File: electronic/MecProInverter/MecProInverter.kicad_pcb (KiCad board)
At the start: 4 copper layers, 104 x 175 mm, 39 parts, among them J1 0022232031, J2 0022232031, J4 Screw_Terminal_01x08, J5 Conn_01x08, J6 LM61, J7 Conn_01x11, K2 RT314A12, Q1 DMN3404L, Q2 DMN3404L, SW1 PTS645SM95SMTR92LFS, SW2 PTS645SM95SMTR92LFS, SW3 PTS645SM95SMTR92LFS, U1 ESP32-S3-MINI-1-N8, U10 CC6904SO-30A, U11 CC6904SO-30A, U12 ACS722xLCTR-40AB, U13 IKCM20L60GA, U14 PSRV05-4MR6T1G, U15 ADUM1201ARZ-RL7, U16 ADUM1201ARZ-RL7, U17 PSRV05-4MR6T1G, U18 PMV100EPAR, U2 ADUM3160, U3 TYPE-C_16PIN_2MD(073), U5 TPS563201DDCR, U6 SKRKAEE020, U7 SKRKAEE020, U8 TLA2528IRTER, U9 CC6904SO-30A

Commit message: Electronic
Power Terminal edit
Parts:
- added D1: LED_3.3V, LED_SMD:LED_0603_1608Metric, F.Cu at (68.7, 169.5)
- added D2: LED_15V, LED_SMD:LED_0603_1608Metric, F.Cu at (68.7, 172.1)
- added H1: MountingHole_Pad, MountingHole:MountingHole_3.2mm_M3_DIN965_Pad_TopBottom, F.Cu at (99.0, 223.0)
- added H2: MountingHole_Pad, MountingHole:MountingHole_3.2mm_M3_DIN965_Pad_TopBottom, F.Cu at (65.6, 164.6)
- added H3: MountingHole_Pad, MountingHole:MountingHole_3.2mm_M3_DIN965_Pad_TopBottom, F.Cu at (193.0, 223.0)
- added H4: MountingHole_Pad, MountingHole:MountingHole_3.2mm_M3_DIN965_Pad_TopBottom, F.Cu at (72.8, 164.6)
- added H5: MountingHole_Pad, MountingHole:MountingHole_3.2mm_M3_DIN965_Pad_TopBottom, F.Cu at (79.9, 157.5)
- added H6: MountingHole_Pad, MountingHole:MountingHole_3.2mm_M3_DIN965_Pad_TopBottom, F.Cu at (79.9, 164.6)
- added J10: Screw_Terminal_01x04, Connector_Phoenix_MC_HighVoltage:PhoenixContact_MCV_1,5_4-G-5.08_1x04_P5.08mm_Vertical, F.Cu at (130.9, 223.7)
- added J3: Screw_Terminal_01x06, Connector_Phoenix_MC_HighVoltage:PhoenixContact_MCV_1,5_6-G-5.08_1x06_P5.08mm_Vertical, F.Cu at (144.3, 251.7)
- added J8: Conn_01x01, Connector_PinHeader_2.54mm:PinHeader_1x01_P2.54mm_Vertical, F.Cu at (64.4, 170.5)
- added J9: Conn_01x01, Connector_PinHeader_2.54mm:PinHeader_1x01_P2.54mm_Vertical, F.Cu at (64.4, 175.2)
- added RV1: 10K, Potentiometer_THT:Potentiometer_Alps_RK09K_Single_Vertical, F.Cu at (98.0, 102.5)
- added TP5: MTCK, TestPoint:TestPoint_Pad_D2.0mm, F.Cu at (53.0, 195.8)
- added TP6: MTDO, TestPoint:TestPoint_Pad_D2.0mm, F.Cu at (53.0, 199.9)
- added TP7: MTMS, TestPoint:TestPoint_Pad_D2.0mm, F.Cu at (53.0, 203.9)
- added TP8: MTDI, TestPoint:TestPoint_Pad_D2.0mm, F.Cu at (53.0, 208.0)
- added U19: PSRV05-4MR6T1G, footprint:SOT-23-6_L2.9-W1.6-P0.95-LS2.8-BL, F.Cu at (48.9, 196.0)
- added U20: PSRV05-4MR6T1G, footprint:SOT-23-6_L2.9-W1.6-P0.95-LS2.8-BL, F.Cu at (48.9, 200.6)
- added U4: LVE2560E, Own_Library:LVE2560E, B.Cu at (140.5, 211.2)
- J1, J2: footprint digikey-footprints:PinHeader_1x3_P2.54mm_Drill1.02mm -> footprint:CONN-TH_3P-P2.54_22-23-2031
- J4: value Screw_Terminal_01x08 -> Screw_Terminal_01x04; footprint Connector_Phoenix_MC_HighVoltage:PhoenixContact_MCV_1,5_8-G-5.08_1x08_P5.08mm_Vertical -> Connector_Phoenix_MC_HighVoltage:PhoenixContact_MCV_1,5_4-G-5.08_1x04_P5.08mm_Vertical
- TP1, TP2, TP3, TP4: footprint Connector_Pin:Pin_D1.0mm_L10.0mm_LooseFit -> TestPoint:TestPoint_Pad_D2.0mm
- U12: value ACS722xLCTR-40AB -> TEA1-0505HI; footprint Package_SO:SOIC-8_3.9x4.9mm_P1.27mm -> Converter_DCDC:Converter_DCDC_TRACO_TEA1HI-xxxx_THT
- moved U12 34.3 mm to (169.5, 214.0), turned to -90 degrees
- moved Q1 30.1 mm to (151.0, 193.0)
- moved D3 17.4 mm to (107.0, 89.0)
- moved U9 17.3 mm to (102.0, 212.0)
- moved U13 16.0 mm to (133.0, 167.0)
- moved PS1 3.00 mm to (102.2, 122.7)
- moved U10 2.24 mm to (102.0, 206.0)
- moved U2 1.00 mm to (182.0, 213.0)
- moved J4 0.34 mm to (108.6, 223.7)
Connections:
- net Net-(U12-VIOUT) renamed +5V
- C2 pad 1: Net-(U13-P) -> Net-(J8-Pin_1)
- C3 pad 1: Net-(U13-P) -> Net-(J8-Pin_1)
- C4 pad 1: Net-(U13-P) -> Net-(J8-Pin_1)
- J4 pad 1: /Power/AC_L -> GND
- J4 pad 2: /Power/AC_N -> /Power/W
- J4 pad 3: Earth -> /Power/V
- J4 pad 4: Earth -> /Power/U
- J7 pad 8: unconnected-(J7-Pin_8-Pad8) -> /Control/UART_TX
- J7 pad 9: unconnected-(J7-Pin_9-Pad9) -> /Control/UART_RX
- U1 pad 10: /Control/FAN1_PWM_FB -> /Control/SW2OUT
- U1 pad 11: /Control/POT1OUT -> /Control/SW3OUT
- U1 pad 12: /Control/RGBLED -> Net-(U1-IO8)
- U1 pad 13: LINW -> Net-(U1-IO9)
- U1 pad 14: LINV -> LINW
- U1 pad 15: LINU -> LINV
- U1 pad 16: HINW -> LINU
- U1 pad 17: HINV -> HINW
- U1 pad 18: HINU -> HINV
- U1 pad 19: RELAY -> HINU
- U1 pad 20: /Control/TEMP_HEATSINK -> RELAY
- U1 pad 21: Net-(U1-IO17) -> /Control/RGBLED
- U1 pad 22: Net-(U1-IO18) -> /Control/TEMP_HEATSINK
- U1 pad 25: unconnected-(U1-IO21-Pad25) -> /Control/ISO_GPIO_1
- U1 pad 26: /Control/SW1OUT -> unconnected-(U1-IO26-Pad26)
- U1 pad 27: unconnected-(U1-IO47-Pad27) -> VFO
- U1 pad 28: /Control/SW2OUT -> ITRIP
- U1 pad 29: /Control/SW3OUT -> /Control/SPI_CS
- U1 pad 31: /Control/SPI_MISO -> /Control/SPI_MOSI
- U1 pad 32: /Control/SPI_MOSI -> /Control/SPI_CLK
- U1 pad 33: /Control/SPI_CLK -> /Control/SPI_MISO
- U1 pad 34: /Control/SPI_CS -> /Control/ISO_GPIO_2
- U1 pad 35: unconnected-(U1-IO39-Pad35) -> Net-(U1-IO39)
- U1 pad 36: unconnected-(U1-IO40-Pad36) -> Net-(U1-IO40)
- U1 pad 37: unconnected-(U1-IO41-Pad37) -> Net-(U1-IO41)
- U1 pad 38: unconnected-(U1-IO42-Pad38) -> Net-(U1-IO42)
- U1 pad 5: unconnected-(U1-IO1-Pad5) -> /Control/FAN_CONTROL
- U1 pad 6: unconnected-(U1-IO2-Pad6) -> /Control/FAN1_PWM_FB
- U1 pad 7: unconnected-(U1-IO3-Pad7) -> /Control/FAN2_PWM_FB
- U1 pad 8: /Control/FAN_CONTROL -> /Control/POT1OUT
- U1 pad 9: /Control/FAN2_PWM_FB -> /Control/SW1OUT
- U12 pad 1: Net-(U13-U) -> +5VD
- U12 pad 2: Net-(U13-U) -> GNDD
- U13 pad 14: unconnected-(U13-VFO-Pad14) -> VFO
- U13 pad 15: unconnected-(U13-ITRIP-Pad15) -> ITRIP
- U13 pad 23: Net-(U13-P) -> Net-(J8-Pin_1)
- U16 pad 2: /Control/ISO_GPIO_3 -> /Control/UART_RX
- U16 pad 3: /Control/ISO_GPIO_4 -> /Control/UART_TX
- U8 pad 6: Net-(U8-AIN7/GPIO7) -> unconnected-(U8-AIN7/GPIO7-Pad6)
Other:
- outline, holes or cut-outs redrawn

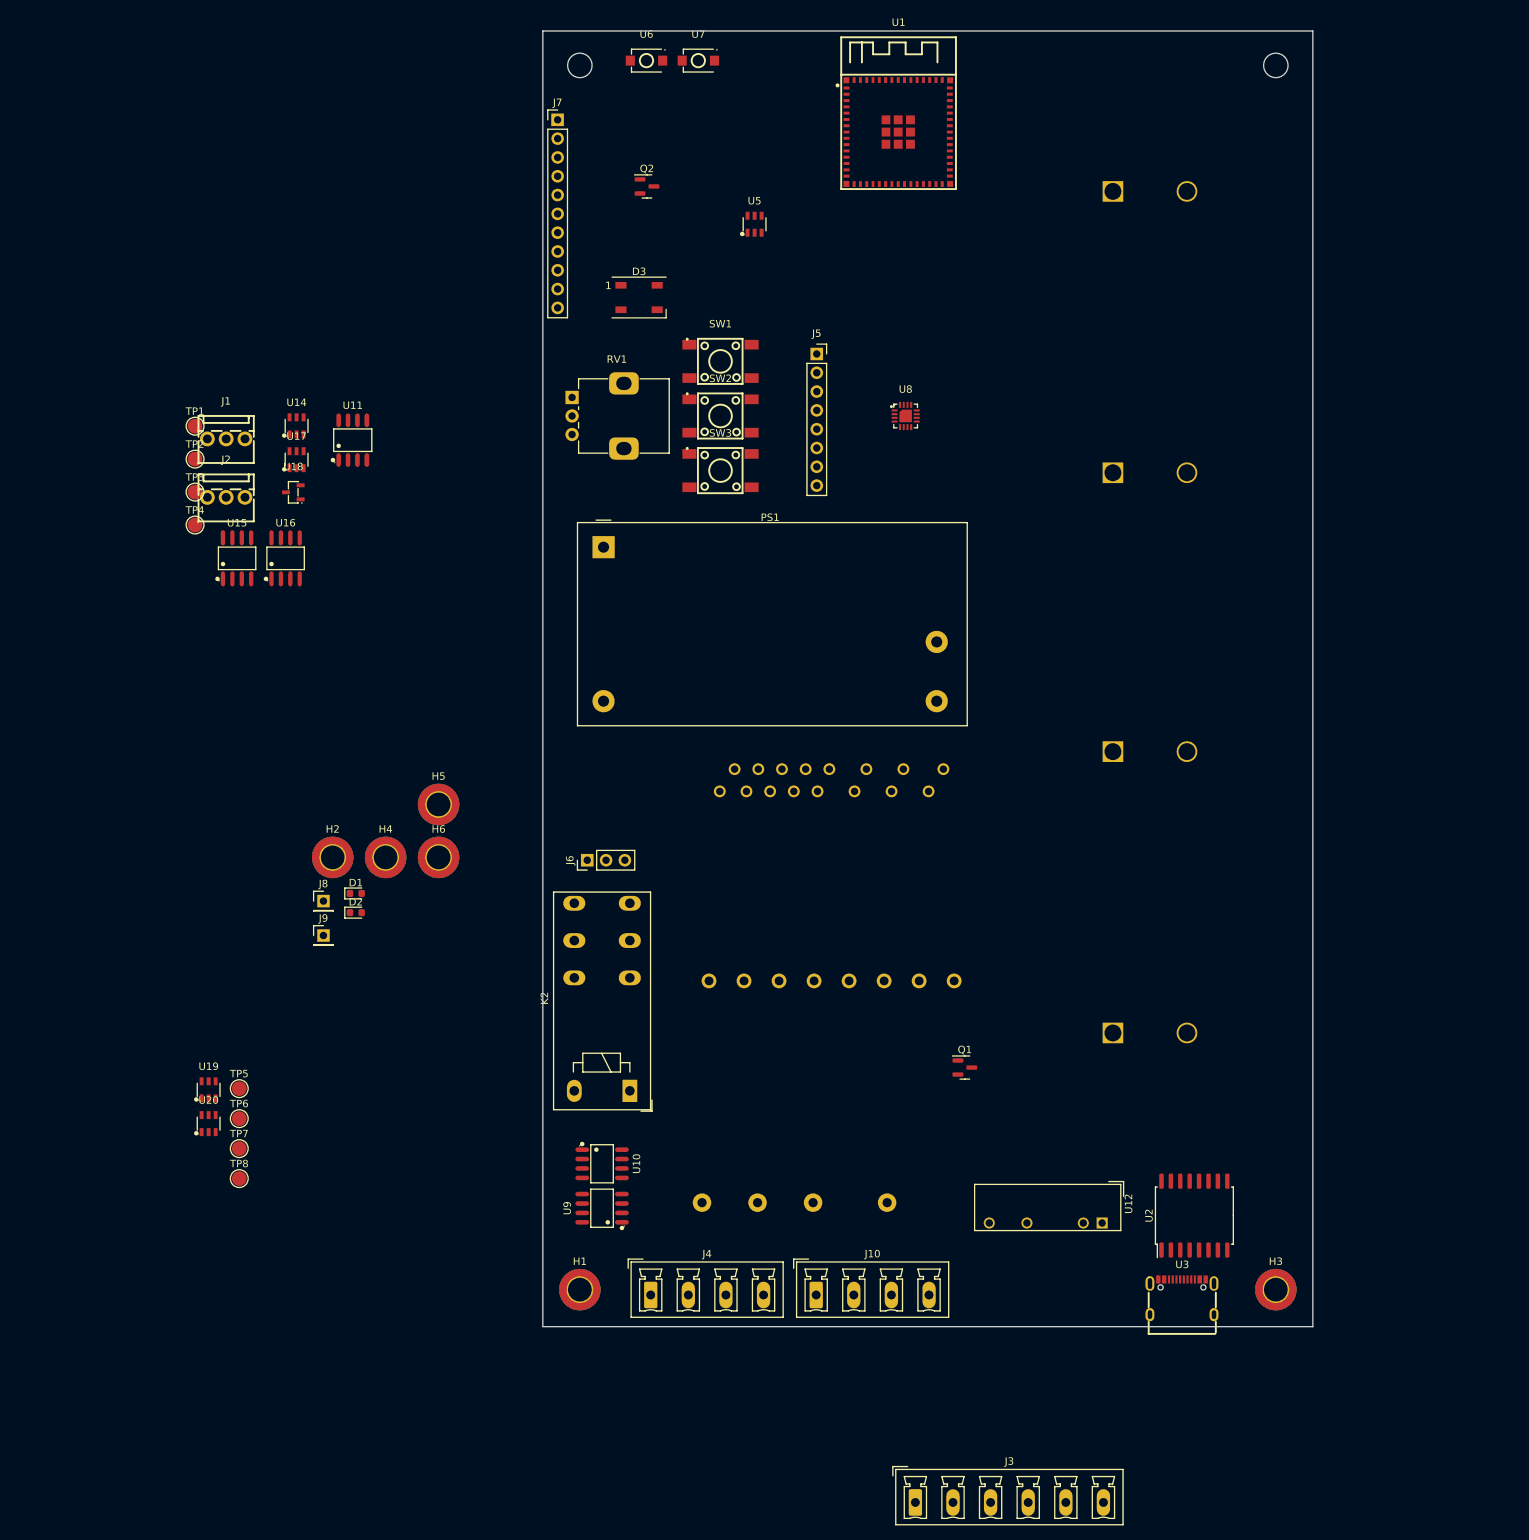
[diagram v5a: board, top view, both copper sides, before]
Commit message: Electronic
Footprint assignment
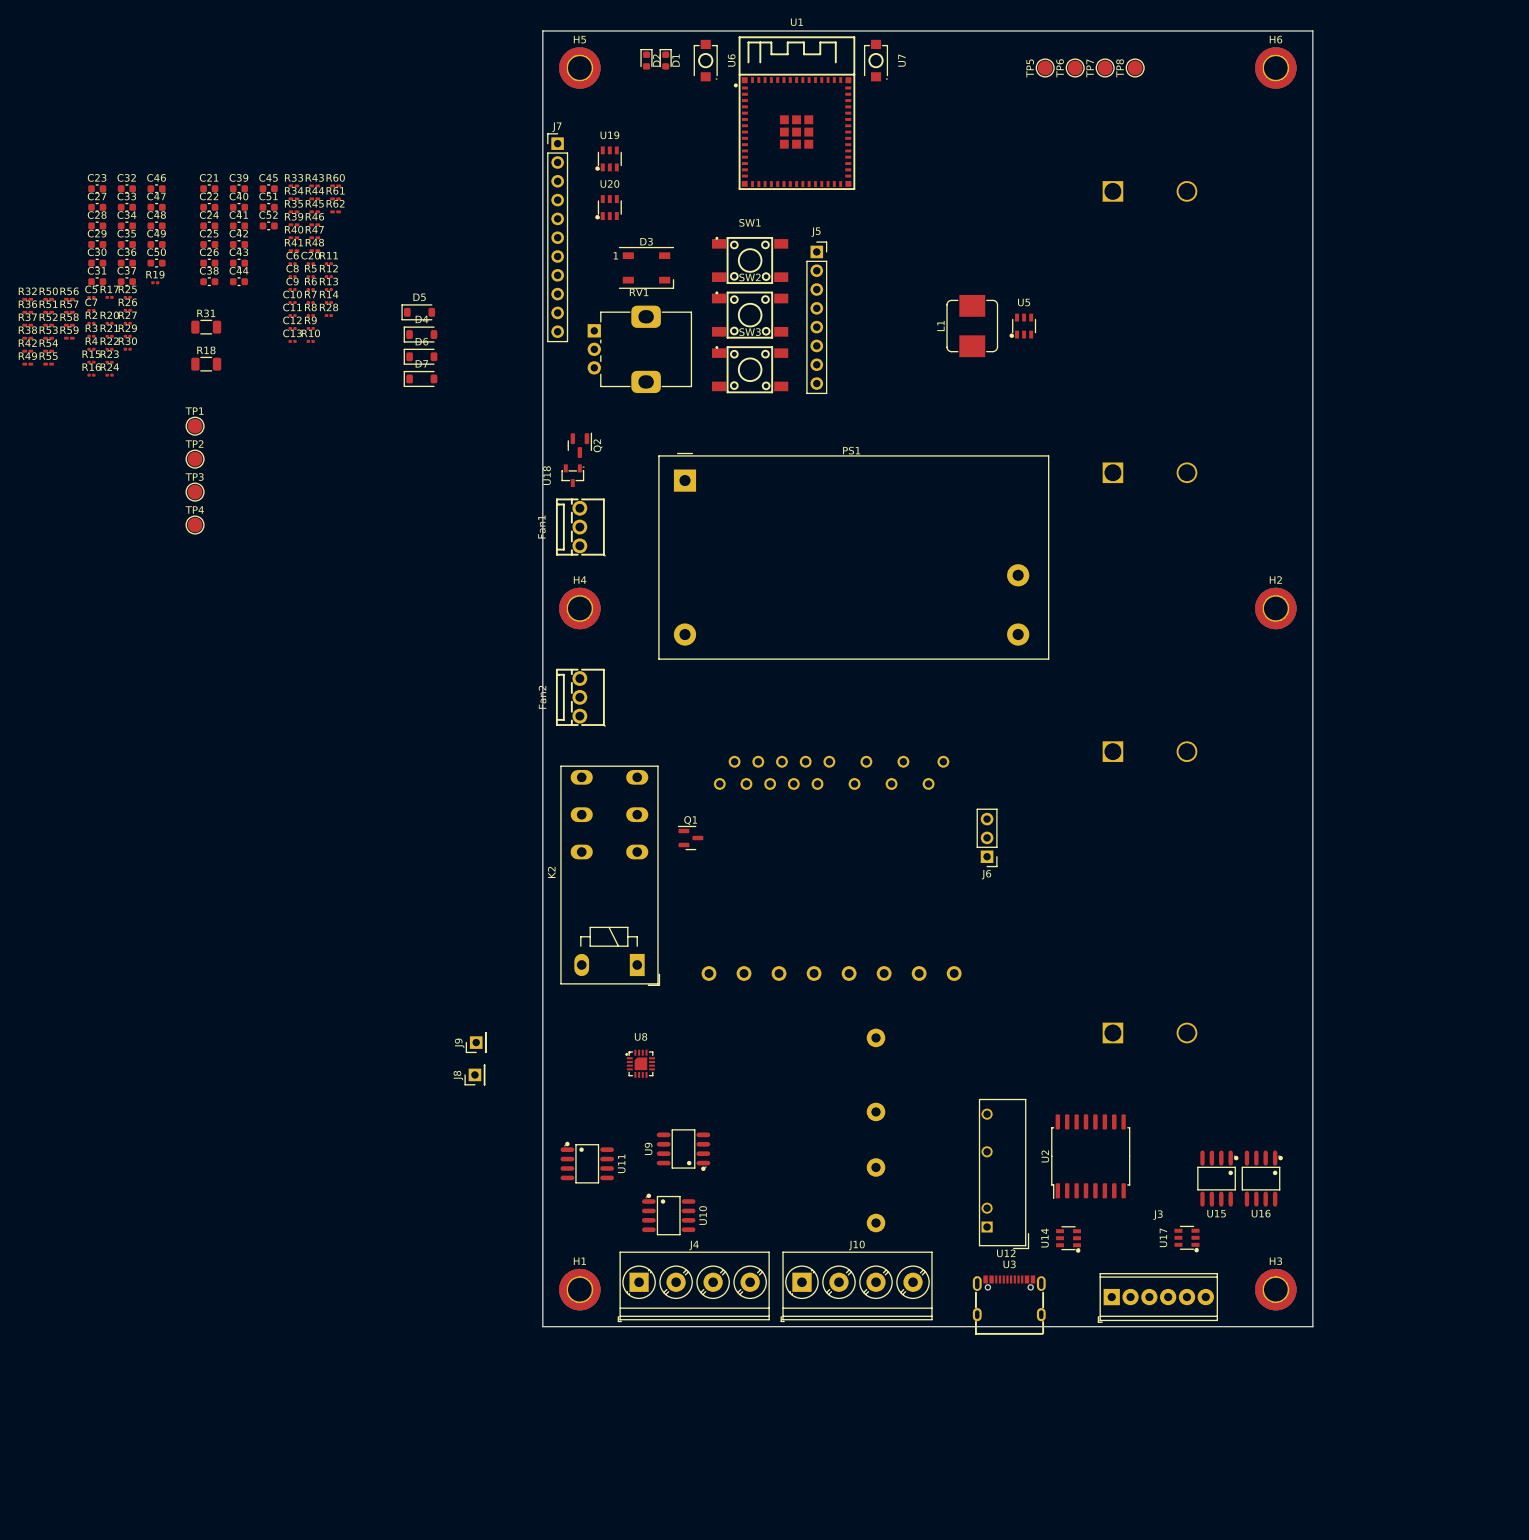
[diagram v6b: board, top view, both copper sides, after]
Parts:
- removed J1, J2: 0022232031, footprint:CONN-TH_3P-P2.54_22-23-2031
- added C10: 10nF, Capacitor_SMD:C_0201_0603Metric, F.Cu at (60.2, 89.7)
- added C11: 10nF, Capacitor_SMD:C_0201_0603Metric, F.Cu at (60.2, 91.4)
- added C12: 10nF, Capacitor_SMD:C_0201_0603Metric, F.Cu at (60.2, 93.2)
- added C13: 10nF, Capacitor_SMD:C_0201_0603Metric, F.Cu at (60.2, 94.9)
- added C20: 10uF, Capacitor_SMD:C_0201_0603Metric, F.Cu at (62.7, 84.4)
- added C21: 100nF, Capacitor_SMD:C_0603_1608Metric, F.Cu at (49.0, 74.3)
- added C22: 10uF, Capacitor_SMD:C_0603_1608Metric, F.Cu at (49.0, 76.8)
- added C23: 100nF, Capacitor_SMD:C_0603_1608Metric, F.Cu at (33.8, 74.3)
- added C24: 100nF, Capacitor_SMD:C_0603_1608Metric, F.Cu at (49.0, 79.3)
- added C25: 22uF, Capacitor_SMD:C_0603_1608Metric, F.Cu at (49.0, 81.8)
- added C26: 100nF, Capacitor_SMD:C_0603_1608Metric, F.Cu at (49.0, 84.3)
- added C27: 22uF, Capacitor_SMD:C_0603_1608Metric, F.Cu at (33.8, 76.8)
- added C28: 1uF, Capacitor_SMD:C_0603_1608Metric, F.Cu at (33.8, 79.3)
- added C29: 1uF, Capacitor_SMD:C_0603_1608Metric, F.Cu at (33.8, 81.8)
- added C30: 1uF, Capacitor_SMD:C_0603_1608Metric, F.Cu at (33.8, 84.3)
- added C31: 1uF, Capacitor_SMD:C_0603_1608Metric, F.Cu at (33.8, 86.9)
- added C32: 1uF, Capacitor_SMD:C_0603_1608Metric, F.Cu at (37.8, 74.3)
- added C33: 100nF, Capacitor_SMD:C_0603_1608Metric, F.Cu at (37.8, 76.8)
- added C34: 100nF, Capacitor_SMD:C_0603_1608Metric, F.Cu at (37.8, 79.3)
- added C35: 100nF, Capacitor_SMD:C_0603_1608Metric, F.Cu at (37.8, 81.8)
- added C36: 100nF, Capacitor_SMD:C_0603_1608Metric, F.Cu at (37.8, 84.3)
- added C37: 10uF, Capacitor_SMD:C_0603_1608Metric, F.Cu at (37.8, 86.9)
- added C38: 220nF, Capacitor_SMD:C_0603_1608Metric, F.Cu at (49.0, 86.9)
- added C39: 220nF, Capacitor_SMD:C_0603_1608Metric, F.Cu at (53.0, 74.3)
- added C40: 22uF, Capacitor_SMD:C_0603_1608Metric, F.Cu at (53.0, 76.8)
- added C41: 0.1nF, Capacitor_SMD:C_0603_1608Metric, F.Cu at (53.0, 79.3)
- added C42: 0.1nF, Capacitor_SMD:C_0603_1608Metric, F.Cu at (53.0, 81.8)
- added C43: 100nF, Capacitor_SMD:C_0603_1608Metric, F.Cu at (53.0, 84.3)
- added C44: 0.1nF, Capacitor_SMD:C_0603_1608Metric, F.Cu at (53.0, 86.9)
- added C45: 100nF, Capacitor_SMD:C_0603_1608Metric, F.Cu at (57.0, 74.3)
- added C46: 100nF, Capacitor_SMD:C_0603_1608Metric, F.Cu at (41.8, 74.3)
- added C47: 100nF, Capacitor_SMD:C_0603_1608Metric, F.Cu at (41.8, 76.8)
- added C48: 100nF, Capacitor_SMD:C_0603_1608Metric, F.Cu at (41.8, 79.3)
- added C49: 100nF, Capacitor_SMD:C_0603_1608Metric, F.Cu at (41.8, 81.8)
- added C5: 100nF, Capacitor_SMD:C_0201_0603Metric, F.Cu at (33.0, 89.0)
- added C50: 1uF, Capacitor_SMD:C_0603_1608Metric, F.Cu at (41.8, 84.3)
- added C51: 100nF, Capacitor_SMD:C_0603_1608Metric, F.Cu at (57.0, 76.8)
- added C52: 1uF, Capacitor_SMD:C_0603_1608Metric, F.Cu at (57.0, 79.3)
- added C6: 100nF, Capacitor_SMD:C_0201_0603Metric, F.Cu at (60.2, 84.4)
- added C7: 1uF, Capacitor_SMD:C_0201_0603Metric, F.Cu at (33.0, 90.7)
- added C8: 10nF, Capacitor_SMD:C_0201_0603Metric, F.Cu at (60.2, 86.2)
- added C9: 10nF, Capacitor_SMD:C_0201_0603Metric, F.Cu at (60.2, 87.9)
- added D4: D, Diode_SMD:D_SOD-123, F.Cu at (77.7, 94.0)
- added D5: D, Diode_SMD:D_SOD-123, F.Cu at (77.3, 91.0)
- added D6: D, Diode_SMD:D_SOD-123, F.Cu at (77.7, 97.0)
- added D7: D, Diode_SMD:D_SOD-123, F.Cu at (77.7, 100.0)
- added Fan1: 0022232031, footprint:CONN-TH_3P-P2.54_22-23-2031, F.Cu at (99.0, 120.0)
- added Fan2: 0022232031, footprint:CONN-TH_3P-P2.54_22-23-2031, F.Cu at (99.0, 143.0)
- added L1: 2.2uH, Inductor_SMD:L_Bourns_SRP7028A_7.3x6.6mm, F.Cu at (152.0, 92.9)
- added R10: 165, Resistor_SMD:R_0201_0603Metric, F.Cu at (62.7, 94.9)
- added R11: 33.2k, Resistor_SMD:R_0201_0603Metric, F.Cu at (65.1, 84.4)
- added R12: 10k, Resistor_SMD:R_0201_0603Metric, F.Cu at (65.1, 86.2)
- added R13: 40, Resistor_SMD:R_0201_0603Metric, F.Cu at (65.1, 87.9)
- added R14: 820, Resistor_SMD:R_0201_0603Metric, F.Cu at (65.1, 89.7)
- added R15: 100K, Resistor_SMD:R_0201_0603Metric, F.Cu at (33.0, 97.7)
- added R16: 100K, Resistor_SMD:R_0201_0603Metric, F.Cu at (33.0, 99.5)
- added R17: 100K, Resistor_SMD:R_0201_0603Metric, F.Cu at (35.5, 89.0)
- added R18: 90, Resistor_SMD:R_1206_3216Metric, F.Cu at (48.5, 98.0)
- added R19: 10k, Resistor_SMD:R_0201_0603Metric, F.Cu at (41.7, 87.0)
- added R2: 121, Resistor_SMD:R_0201_0603Metric, F.Cu at (33.0, 92.5)
- added R20: 1K, Resistor_SMD:R_0201_0603Metric, F.Cu at (35.5, 92.5)
- added R21: 1K, Resistor_SMD:R_0201_0603Metric, F.Cu at (35.5, 94.2)
- added R22: 1k, Resistor_SMD:R_0201_0603Metric, F.Cu at (35.5, 96.0)
- added R23: 10k, Resistor_SMD:R_0201_0603Metric, F.Cu at (35.5, 97.7)
- added R24: 1.6k, Resistor_SMD:R_0201_0603Metric, F.Cu at (35.5, 99.5)
- added R25: 1.6k, Resistor_SMD:R_0201_0603Metric, F.Cu at (37.9, 89.0)
- added R26: 121, Resistor_SMD:R_0201_0603Metric, F.Cu at (37.9, 90.7)
- added R27: 121, Resistor_SMD:R_0201_0603Metric, F.Cu at (37.9, 92.5)
- added R28: 100k, Resistor_SMD:R_0201_0603Metric, F.Cu at (65.1, 91.4)
- added R29: 121, Resistor_SMD:R_0201_0603Metric, F.Cu at (37.9, 94.2)
- added R3: 121, Resistor_SMD:R_0201_0603Metric, F.Cu at (33.0, 94.2)
- added R30: 121, Resistor_SMD:R_0201_0603Metric, F.Cu at (37.9, 96.0)
- added R31: 0, Resistor_SMD:R_1206_3216Metric, F.Cu at (48.5, 93.0)
- added R32: 121, Resistor_SMD:R_0201_0603Metric_Pad0.64x0.40mm_HandSolder, F.Cu at (24.4, 89.2)
- added R33: 1.8k, Resistor_SMD:R_0201_0603Metric_Pad0.64x0.40mm_HandSolder, F.Cu at (60.4, 73.9)
- added R34: 10k, Resistor_SMD:R_0201_0603Metric_Pad0.64x0.40mm_HandSolder, F.Cu at (60.4, 75.7)
- added R35: 999m, Resistor_SMD:R_0201_0603Metric_Pad0.64x0.40mm_HandSolder, F.Cu at (60.4, 77.4)
- added R36: 24, Resistor_SMD:R_0201_0603Metric_Pad0.64x0.40mm_HandSolder, F.Cu at (24.4, 91.0)
- added R37: 24, Resistor_SMD:R_0201_0603Metric_Pad0.64x0.40mm_HandSolder, F.Cu at (24.4, 92.8)
- added R38: 165, Resistor_SMD:R_0201_0603Metric_Pad0.64x0.40mm_HandSolder, F.Cu at (24.4, 94.5)
- added R39: 33k, Resistor_SMD:R_0201_0603Metric_Pad0.64x0.40mm_HandSolder, F.Cu at (60.4, 79.2)
- added R4: 121, Resistor_SMD:R_0201_0603Metric, F.Cu at (33.0, 96.0)
- added R40: 10k, Resistor_SMD:R_0201_0603Metric_Pad0.64x0.40mm_HandSolder, F.Cu at (60.4, 80.9)
- added R41: 10k, Resistor_SMD:R_0201_0603Metric_Pad0.64x0.40mm_HandSolder, F.Cu at (60.4, 82.7)
- added R42: 4.7k, Resistor_SMD:R_0201_0603Metric_Pad0.64x0.40mm_HandSolder, F.Cu at (24.4, 96.2)
- added R43: 100, Resistor_SMD:R_0201_0603Metric_Pad0.64x0.40mm_HandSolder, F.Cu at (63.2, 73.9)
- added R44: 100, Resistor_SMD:R_0201_0603Metric_Pad0.64x0.40mm_HandSolder, F.Cu at (63.2, 75.7)
- added R45: 100, Resistor_SMD:R_0201_0603Metric_Pad0.64x0.40mm_HandSolder, F.Cu at (63.2, 77.4)
- added R46: 100k, Resistor_SMD:R_0201_0603Metric_Pad0.64x0.40mm_HandSolder, F.Cu at (63.2, 79.2)
- added R47: 820, Resistor_SMD:R_0201_0603Metric_Pad0.64x0.40mm_HandSolder, F.Cu at (63.2, 80.9)
- added R48: 165, Resistor_SMD:R_0201_0603Metric_Pad0.64x0.40mm_HandSolder, F.Cu at (63.2, 82.7)
- added R49: 180, Resistor_SMD:R_0201_0603Metric_Pad0.64x0.40mm_HandSolder, F.Cu at (24.4, 98.0)
- added R5: 165, Resistor_SMD:R_0201_0603Metric, F.Cu at (62.7, 86.2)
- added R50: 180, Resistor_SMD:R_0201_0603Metric_Pad0.64x0.40mm_HandSolder, F.Cu at (27.2, 89.2)
- added R51: 180, Resistor_SMD:R_0201_0603Metric_Pad0.64x0.40mm_HandSolder, F.Cu at (27.2, 91.0)
- added R52: 180, Resistor_SMD:R_0201_0603Metric_Pad0.64x0.40mm_HandSolder, F.Cu at (27.2, 92.8)
- added R53: 0, Resistor_SMD:R_0201_0603Metric_Pad0.64x0.40mm_HandSolder, F.Cu at (27.2, 94.5)
- added R54: 0, Resistor_SMD:R_0201_0603Metric_Pad0.64x0.40mm_HandSolder, F.Cu at (27.2, 96.2)
- added R55: 0, Resistor_SMD:R_0201_0603Metric_Pad0.64x0.40mm_HandSolder, F.Cu at (27.2, 98.0)
- added R56: 0, Resistor_SMD:R_0201_0603Metric_Pad0.64x0.40mm_HandSolder, F.Cu at (30.1, 89.2)
- added R57: 10k, Resistor_SMD:R_0201_0603Metric_Pad0.64x0.40mm_HandSolder, F.Cu at (30.1, 91.0)
- added R58: 10k, Resistor_SMD:R_0201_0603Metric_Pad0.64x0.40mm_HandSolder, F.Cu at (30.1, 92.8)
- added R59: 10k, Resistor_SMD:R_0201_0603Metric_Pad0.64x0.40mm_HandSolder, F.Cu at (30.1, 94.5)
- added R6: 165, Resistor_SMD:R_0201_0603Metric, F.Cu at (62.7, 87.9)
- added R60: 999m, Resistor_SMD:R_0201_0603Metric_Pad0.64x0.40mm_HandSolder, F.Cu at (66.0, 73.9)
- added R61: 3.3k, Resistor_SMD:R_0201_0603Metric_Pad0.64x0.40mm_HandSolder, F.Cu at (66.0, 75.7)
- added R62: 10k, Resistor_SMD:R_0201_0603Metric_Pad0.64x0.40mm_HandSolder, F.Cu at (66.0, 77.4)
- added R7: 165, Resistor_SMD:R_0201_0603Metric, F.Cu at (62.7, 89.7)
- added R8: 165, Resistor_SMD:R_0201_0603Metric, F.Cu at (62.7, 91.4)
- added R9: 165, Resistor_SMD:R_0201_0603Metric, F.Cu at (62.7, 93.2)
- H1, H3, H4, H5, H6: value MountingHole_Pad -> ~
- H2: value MountingHole_Pad -> locked
- J10: value Screw_Terminal_01x04 -> Net; footprint Connector_Phoenix_MC_HighVoltage:PhoenixContact_MCV_1,5_4-G-5.08_1x04_P5.08mm_Vertical -> TerminalBlock_Phoenix:TerminalBlock_Phoenix_PT-1,5-4-5.0-H_1x04_P5.00mm_Horizontal
- J3: value Screw_Terminal_01x06 -> ISO_Data; footprint Connector_Phoenix_MC_HighVoltage:PhoenixContact_MCV_1,5_6-G-5.08_1x06_P5.08mm_Vertical -> TerminalBlock_Phoenix:TerminalBlock_Phoenix_MPT-0,5-6-2.54_1x06_P2.54mm_Horizontal
- J4: value Screw_Terminal_01x04 -> Motor; footprint Connector_Phoenix_MC_HighVoltage:PhoenixContact_MCV_1,5_4-G-5.08_1x04_P5.08mm_Vertical -> TerminalBlock_Phoenix:TerminalBlock_Phoenix_PT-1,5-4-5.0-H_1x04_P5.00mm_Horizontal
- J5: value Conn_01x08 -> Display
- J6: value LM61 -> MAX312820
- J7: value Conn_01x11 -> Test
- J8: value Conn_01x01 -> U_ZK
- J9: value Conn_01x01 -> U_VS
- moved TP8 192.7 mm to (174.0, 58.0), turned to 90 degrees
- moved TP7 187.0 mm to (169.9, 58.0), turned to 90 degrees
- moved TP6 181.3 mm to (165.9, 58.0), turned to 90 degrees
- moved TP5 175.6 mm to (161.8, 58.0), turned to 90 degrees
- moved U17 159.7 mm to (181.0, 216.0), turned to 90 degrees
- moved U15 156.6 mm to (185.0, 208.0), turned to 180 degrees
- moved U16 156.1 mm to (191.0, 208.0), turned to 180 degrees
- moved H6 155.4 mm to (193.0, 58.0)
- moved U14 151.3 mm to (165.0, 216.1), turned to 90 degrees
- moved U19 136.9 mm to (103.1, 70.3)
- moved U20 135.1 mm to (103.1, 76.9)
- moved H2 131.7 mm to (193.0, 131.0)
- moved D2 121.6 mm to (108.0, 57.0), turned to -90 degrees
- moved D1 120.0 mm to (110.6, 57.0), turned to -90 degrees
- moved U11 102.7 mm to (100.0, 206.0), turned to -90 degrees
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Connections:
- C1 pad 1: Net-(U13-P) -> Net-(J8-Pin_1)
- U8 pad 16: +3.3V -> Net-(U8-AIN1/GPIO1)
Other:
- outline, holes or cut-outs redrawn
